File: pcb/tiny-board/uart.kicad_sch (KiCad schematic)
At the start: 14 parts, among them J3 Serial, J6 UART1, U8 W65C51NxP, U9 MAX232, Y1 1.8432 MHz

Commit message: Saving tiny board design
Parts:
- added U7: CD74HC688, Package_DIP:DIP-20_W7.62mm_Socket, symbol 74xx:74HC688
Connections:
- net GND: now also U7.10 (GND), U7.12 (R4), U7.14 (R5), U7.16 (R6), U7.18 (R7), U7.2 (P0), U7.3 (R0), U7.4 (P1), U7.5 (R1), U7.9 (R3)
- net VCC: now also U7.20 (VCC), U7.7 (R2)
- net ~{UART_CS2}: no longer names the net of U8.3 (~{CS2})
- net ~{UART_CS2}: now also U7.19 (P=R)
- new net A2: U7.6 (P2)
- new net A3: U7.8 (P3)
- new net A4: U7.11 (P4)
- new net A5: U7.13 (P5)
- new net A6: U7.15 (P6)
- new net A7: U7.17 (P7)
- new net ~{I/O}: U7.1 (G)
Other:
- note added: "0x7F04-0x7F07"
- moved on the sheet: C12, C13, C15, C16, C18, C19, J3, J6, R7, R8, U8, U9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

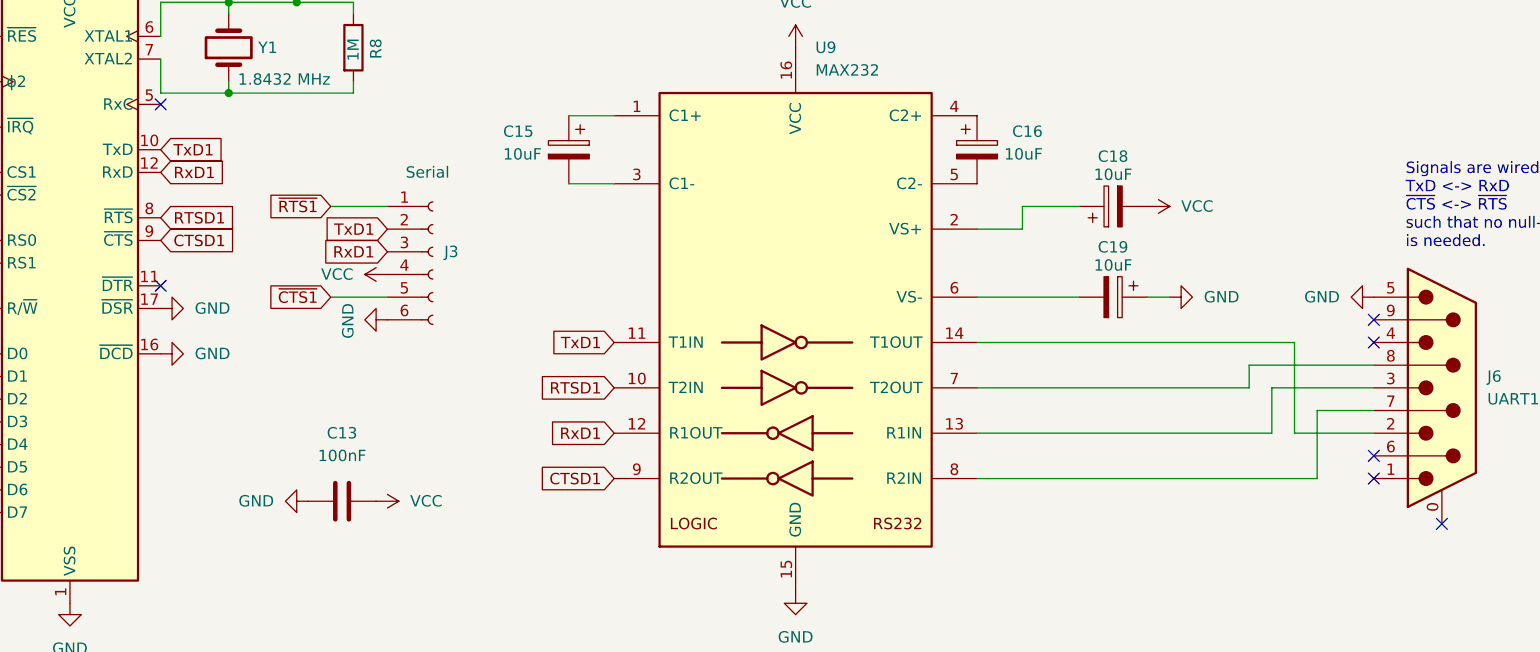
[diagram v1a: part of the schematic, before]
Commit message: Revising TINY board and creating test ROM for TINY board
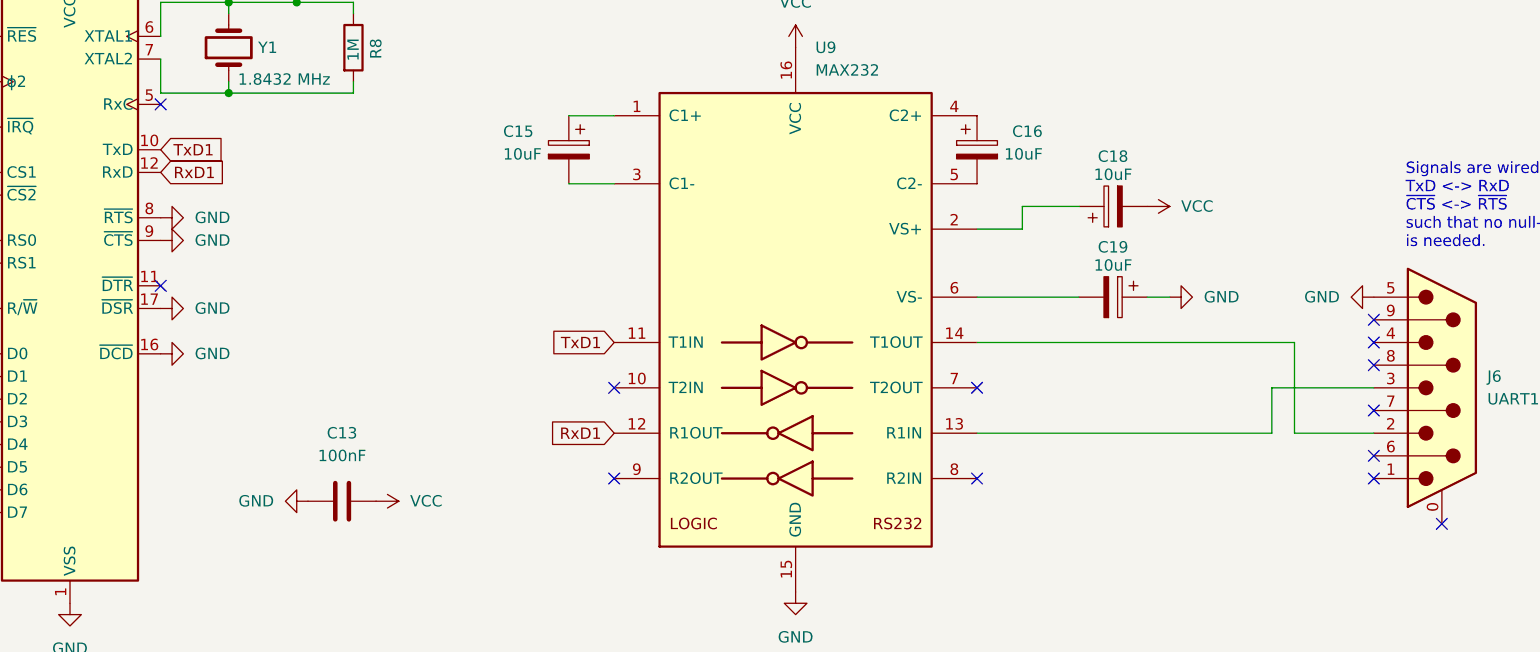
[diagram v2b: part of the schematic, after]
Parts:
- removed J3: Serial, Connector_PinSocket_2.54mm:PinSocket_1x06_P2.54mm_Vertical, symbol Connector:Conn_01x06_Socket
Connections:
- net GND: now also U8.8 (~{RTS}), U8.9 (~{CTS})
- net at U9.7 (T2OUT): no longer J6.8
- net at U9.8 (R2IN): no longer J6.7
- net CTSD1: no longer names the net of U9.9 (R2OUT)
- net CTSD1: no longer U8.9 (~{CTS})
- net RTSD1: no longer names the net of U9.10 (T2IN)
- net RTSD1: no longer U8.8 (~{RTS})
- no-connect marks 7 -> 13

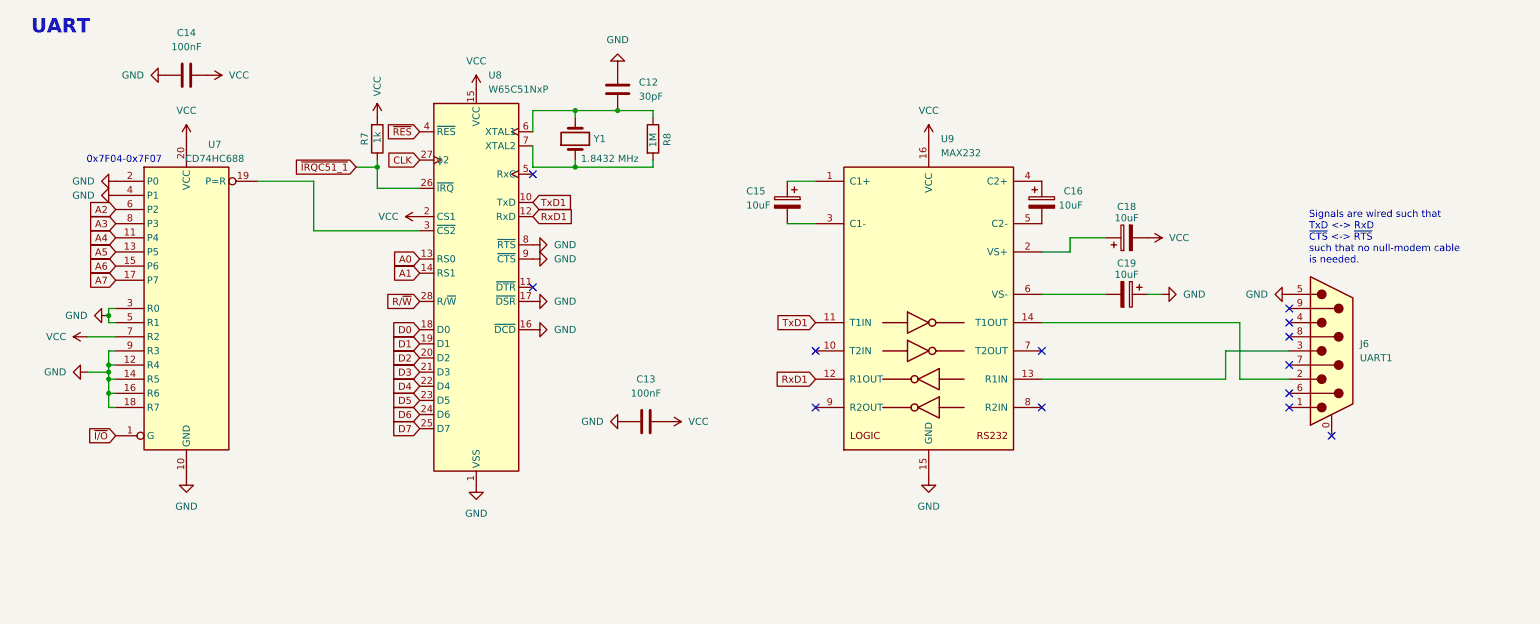
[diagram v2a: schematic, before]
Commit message: Revising TINY board and writing CUPL
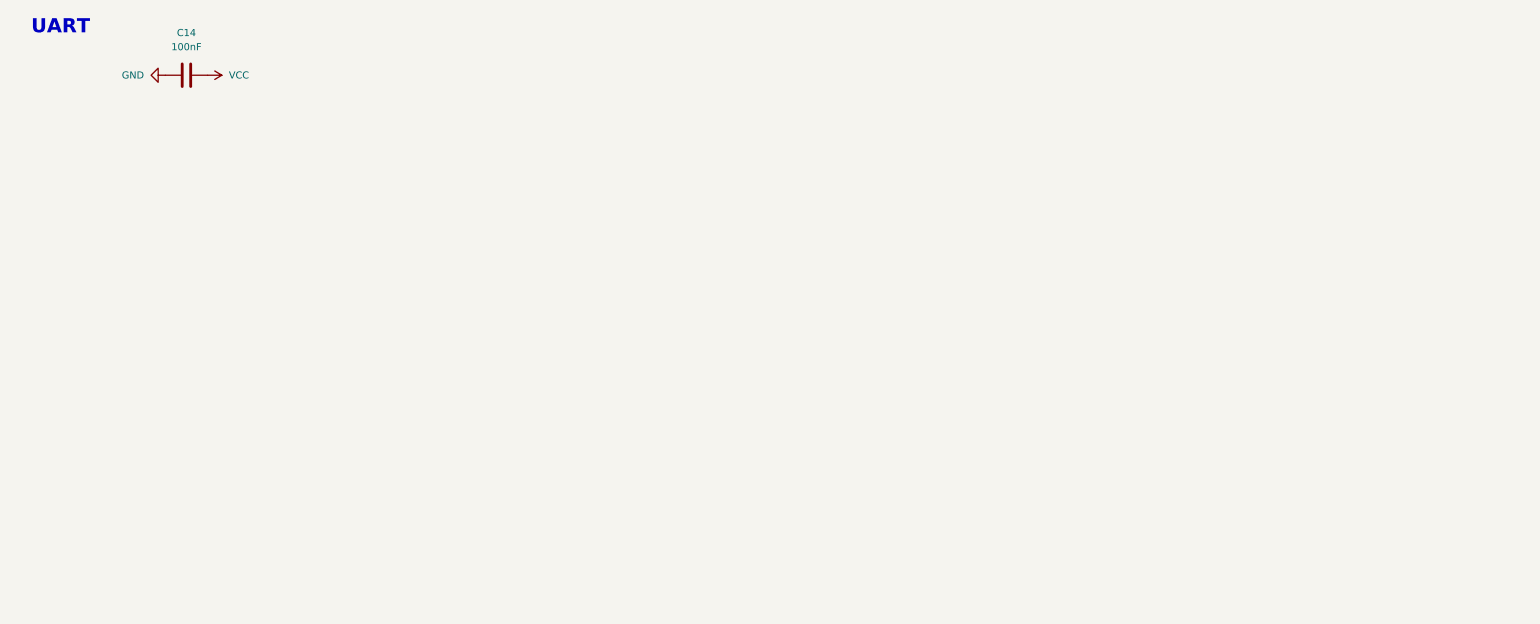
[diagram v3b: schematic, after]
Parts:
- removed C12: 30pF, Capacitor_THT:C_Disc_D5.0mm_W2.5mm_P5.00mm, symbol Device:C
- removed C13: 100nF, Capacitor_THT:C_Disc_D5.0mm_W2.5mm_P5.00mm, symbol Device:C
- removed C15, C16, C18, C19: 10uF, Capacitor_THT:CP_Radial_D5.0mm_P2.50mm, symbol Device:C_Polarized
- removed J6: UART1, Connector_Dsub:DSUB-9_Male_Horizontal_P2.77x2.84mm_EdgePinOffset4.94mm_Housed_MountingHolesOffset7.48mm, symbol Connector:DE9_Plug_MountingHoles
- removed R7: 1k, Resistor_THT:R_Axial_DIN0207_L6.3mm_D2.5mm_P7.62mm_Horizontal, symbol Device:R
- removed R8: 1M, Resistor_THT:R_Axial_DIN0207_L6.3mm_D2.5mm_P7.62mm_Horizontal, symbol Device:R
- removed U7: CD74HC688, Package_DIP:DIP-20_W7.62mm_Socket, symbol 74xx:74HC688
- removed U8: W65C51NxP, Package_DIP:DIP-28_W15.24mm_Socket, symbol 65xx-library:W65C51NxP
- removed U9: MAX232, Package_DIP:DIP-16_W7.62mm_Socket, symbol Interface_UART:MAX232
- removed Y1: 1.8432 MHz, Crystal:Crystal_HC50_Vertical, symbol Device:Crystal
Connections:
- no-connect marks 13 -> 0
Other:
- note removed: "0x7F04-0x7F07"
- note removed: "Signals are wired such that TxD <-> RxD ~{CTS} <-> ~{RTS} such that no null-modem cable is needed."
